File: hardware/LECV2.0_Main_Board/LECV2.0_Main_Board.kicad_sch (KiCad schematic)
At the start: 21 parts, among them J1 LED Indicator Connector, J10 Conn_01x02, J12 Radio, J2 Ox Main, J3 Fuel Main, J4 DAQ HAT Connector, U1 Pico, U2 INA237_Module, U4 W25Q128JVSIQ, U5 Adafruit LSM6DSOX + LIS3MDL

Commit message: Added name to schematic
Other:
- company: (none) -> Missouri S&T Rocket Design Team
- title: (none) -> LECV2.0 Main Board
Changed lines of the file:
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@@
 	(generator_version "9.0")
 	(paper "A3")
+	(title_block
+		(title "LECV2.0 Main Board")
+		(company "Missouri S&T Rocket Design Team")
+		(comment 1 "Author: Rakshak Sudhakaran")
+	)
 	(rectangle
 		(start 170.18 199.39)

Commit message: Temp commit to upload changes to buck converter circuit
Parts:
- added C11: 150u, EEUFC1H151B:CAPPRD500W60D1000H1600, symbol Device:C_Polarized
- added C9: 220n, Capacitor_SMD:C_0805_2012Metric, symbol Device:C
- added R7, R9: 1k, Resistor_SMD:R_0603_1608Metric, symbol Device:R_US
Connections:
- net 11.1V: now also C11.1, C9.1
- net GND: now also C11.2
- net at J3.3 (Pin_3), R1.1: now also R9.2; no longer U1.27 (GPIO21)
- net at J2.3 (Pin_3), R3.1: now also R7.2; no longer U1.29 (GPIO22)
- net at J10.2 (Pin_2), U2. (Vin+): now also C9.2
- new net: R9.1, U1.27 (GPIO21)
- new net: R7.1, U1.29 (GPIO22)
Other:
- moved on the sheet: C18, C22, C24, D1, J1, J10, J2, J3, J4, MOSFET1, R1, R2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

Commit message: Implemented fixes. Ready for 2nd review
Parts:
- added F1: Fuse, Fuse:Fuse_1206_3216Metric, symbol Device:Fuse
- added Q1: BUK6Y33-60PX, BUK6Y33-60PX:LFPAK_SOT669_NEX, symbol BUK6Y33-60PX:BUK6Y33-60PX
- added Q2: Q_NPN, Package_TO_SOT_SMD:SOT-323_SC-70, symbol Device:Q_NPN
- R7, R9: value 1k -> 10K; DigiKey https://www.digikey.com/en/products/detail/vishay-dale/TNPW06031K00BEEA/1606767 -> https://www.digikey.com/en/products/detail/vishay-dale/TNPW060310K0BEEA/1606881
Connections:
- net 11.1V: now also R9.1, Q1.1 (S), Q1.2 (S), Q1.3 (S); no longer C18.1, C22.1, J2.1 (Pin_1), J3.1 (Pin_1)
- net GND: now also Q2.E
- net at J3.3 (Pin_3), R1.1: now also U1.27 (GPIO21); no longer R9.2
- net at J2.3 (Pin_3), R3.1: now also U1.29 (GPIO22); no longer R7.2
- net at R7.1: now also Q2.B; no longer U1.29 (GPIO22)
- net GPIO0 (Servo_PWR_Switch): now reaches U1.4 (GPIO2)
- net GPIO0 (Servo_PWR_Switch): now also R7.2
- new net: Q1.4 (G), Q2.C, R9.2
- new net: C18.1, C22.1, J2.1 (Pin_1), J3.1 (Pin_1), Q1.5 (D)
- new net: C9.2, F1.1, U2. (Vin+)
- new net: F1.2, J10.2 (Pin_2)
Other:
- note added: "Servomotor Power Switch"
- moved on the sheet: C18, C22, C3, J10, J12, J2, J3, U4

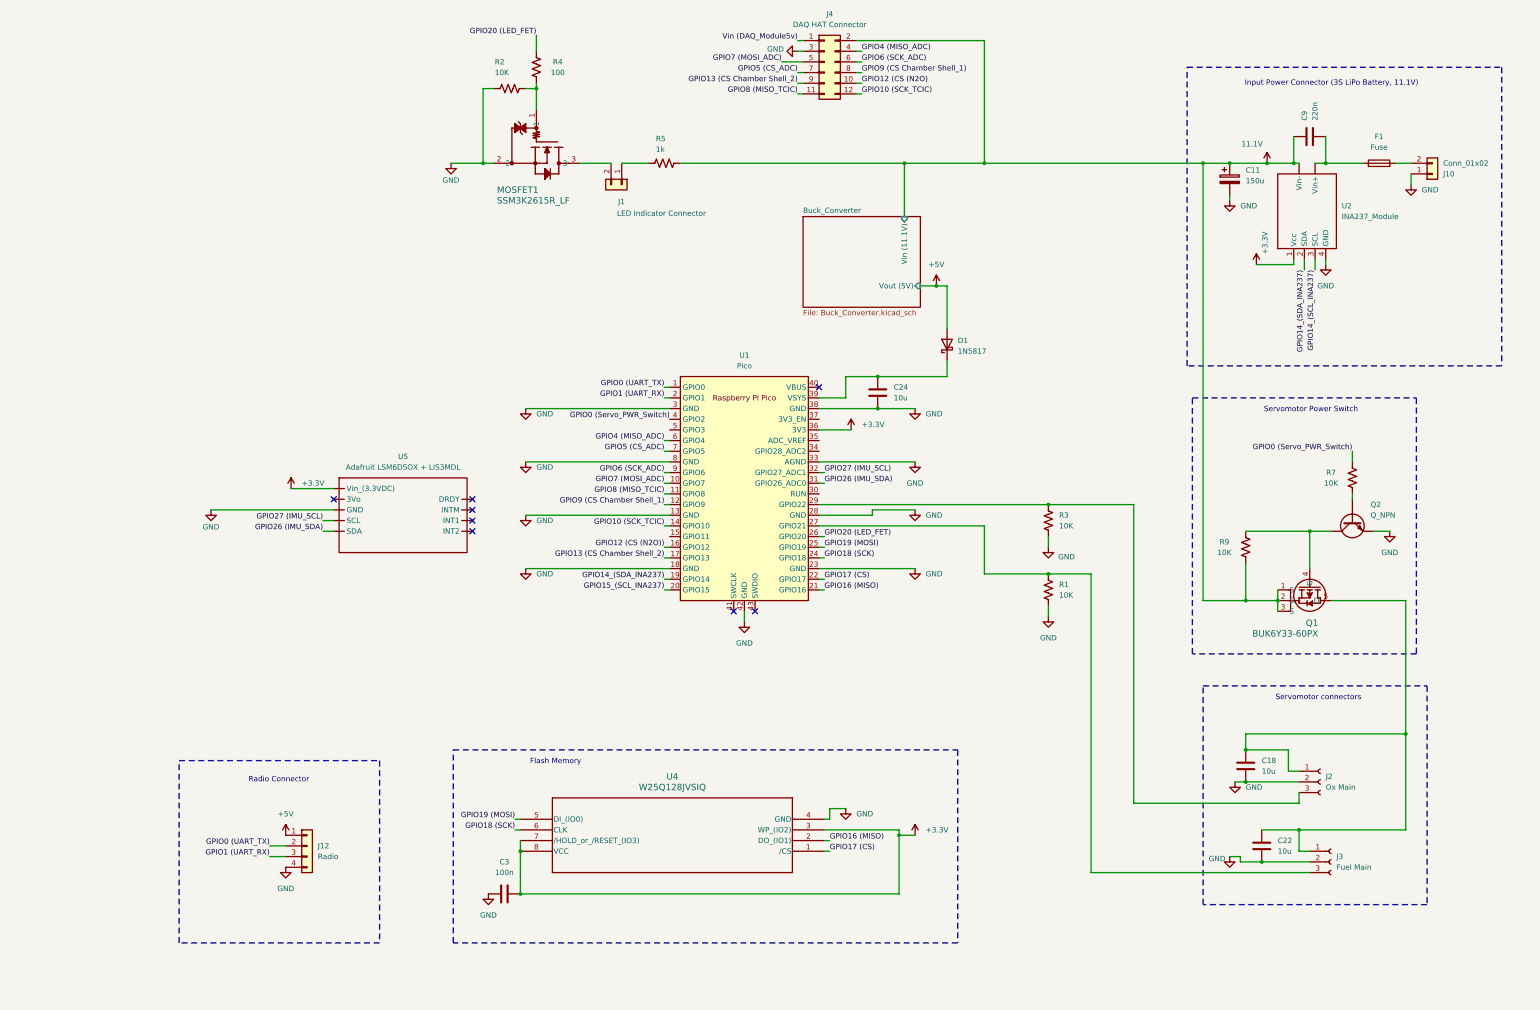
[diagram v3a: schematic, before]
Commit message: Intermediate commit, need to fix servo connector footprints
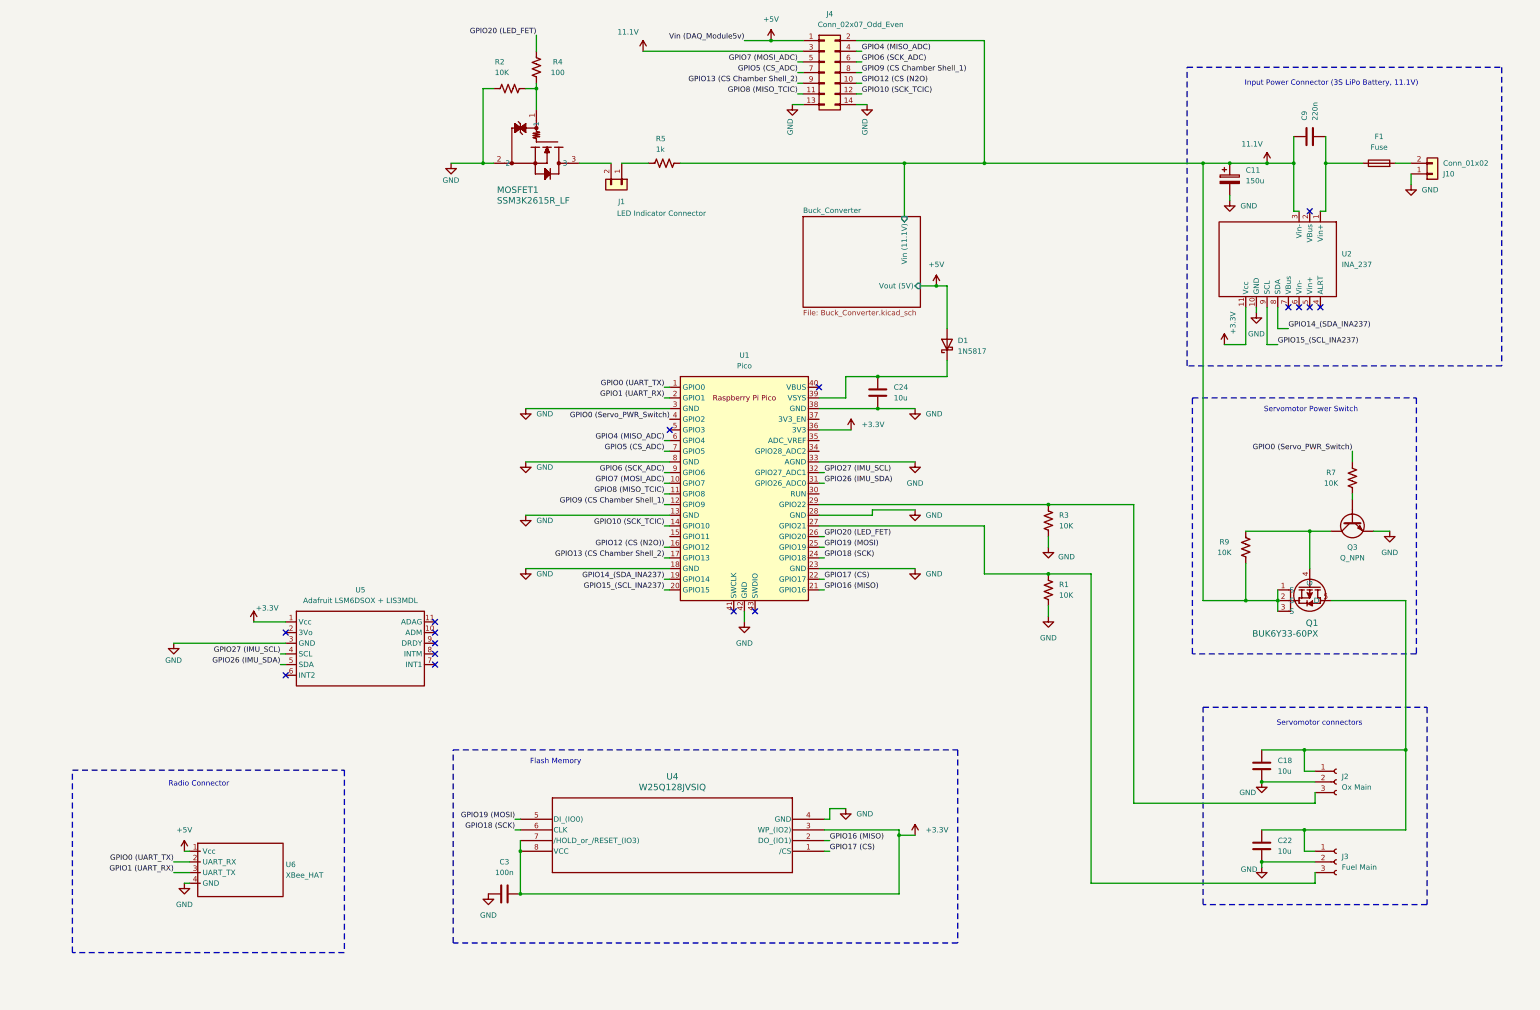
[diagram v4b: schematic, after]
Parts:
- removed J12: Radio, symbol Connector_Generic:Conn_01x04
- removed J4: DAQ HAT Connector, Connector_PinHeader_2.54mm:PinHeader_2x06_P2.54mm_Vertical, symbol Connector_Generic:Conn_02x06_Odd_Even
- removed Q2: Q_NPN, Package_TO_SOT_SMD:SOT-323_SC-70, symbol Device:Q_NPN
- added J4: Conn_02x07_Odd_Even, Connector_PinHeader_2.54mm:PinHeader_2x07_P2.54mm_Vertical, symbol Connector_Generic:Conn_02x07_Odd_Even
- added Q3: Q_NPN, Package_TO_SOT_SMD:SOT-323_SC-70, symbol Device:Q_NPN
- added U6: XBee_HAT, XBee_HAT:XBee-HAT, symbol XBee_HAT:XBee_HAT
- J2, J3: footprint (none) -> Connector_PinHeader_2.54mm:PinHeader_1x03_P2.54mm_Vertical
- U2: value INA237_Module -> INA_237; footprint (none) -> INA_238:INA238_MODULE
- U5: footprint (none) -> Adafruit_LSM6DSOX+LIS3MDL:Adafruit_LSM6DSOX+LIS3MDL
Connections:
- net GPIO14_(SCL_INA237) is gone; now on net 11.1V: U2.3 (Vin-)
- net +3.3V: now also U2.11 (Vcc), U5.1 (Vcc); no longer U2.1 (Vcc), U5. (INT2)
- net +5V: now also J4.1 (Pin_1), U6.1 (Vcc)
- net 11.1V: now also J4.2 (Pin_2), J4.3 (Pin_3); no longer U2. (Vin+)
- net GND: now also U2.10 (GND), U5.3 (GND), J4.13 (Pin_13), J4.14 (Pin_14), Q3.2 (E), U6.4 (GND); no longer U2.4 (GND), U5. (INT2)
- net GPIO0 (UART_TX): now also U6.2 (UART_RX)
- net GPIO1 (UART_RX): now also U6.3 (UART_TX)
- net GPIO10 (SCK_TCIC): now also J4.12 (Pin_12)
- net GPIO12 (CS (N2O): now also J4.10 (Pin_10)
- net GPIO13 (CS Chamber Shell_2): now also J4.9 (Pin_9)
- net GPIO14_(SDA_INA237): now also U2.8 (SDA); no longer U2.2 (SDA)
- net GPIO15_(SCL_INA237): now also U2.9 (SCL)
- net GPIO26 (IMU_SDA): now also U5.5 (SDA); no longer U5. (INT2)
- net GPIO27 (IMU_SCL): now also U5.4 (SCL); no longer U5. (INT2)
- net GPIO4 (MISO_ADC): now also J4.4 (Pin_4)
- net GPIO5 (CS_ADC): now also J4.7 (Pin_7)
- net GPIO6 (SCK_ADC): now also J4.6 (Pin_6)
- net GPIO7 (MOSI_ADC): now also J4.5 (Pin_5)
- net GPIO8 (MISO_TCIC): now also J4.11 (Pin_11)
- net GPIO9 (CS Chamber Shell_1): now also J4.8 (Pin_8)
- net at Q1.4 (G), R9.2: now also Q3.3 (C)
- net at C9.2, F1.1: now also U2.1 (Vin+); no longer U2. (Vin+)
- net at R7.1: now also Q3.1 (B)
- no-connect marks 8 -> 16
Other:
- moved on the sheet: C18, J2, J3

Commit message: Fixed all footprints. Defined PCB edge, arbitrarily placed components
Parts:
- J2, J3: footprint Connector_PinHeader_2.54mm:PinHeader_1x03_P2.54mm_Vertical -> 54-00440:TENSILITY_54-00440; DigiKey (none) -> https://www.digikey.com/en/products/detail/tensility-intern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
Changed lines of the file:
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@@
 			)
 		)
-		(property "Footprint" "Connector_PinHeader_2.54mm:PinHeader_1x03_P2.54mm_Vertical"
+		(property "Footprint" "54-00440:TENSILITY_54-00440"
 			(at 358.14 203.2 0)
 			(effects
@@
 			)
 		)
-		(property "Datasheet" "~"
+		(property "Datasheet" "https://tensility.s3.us-west-2.amazonaws.com/uploads/pdffiles/54-00440.pdf"
 			(at 358.14 203.2 0)
 			(effects
@@
 		)
 		(property "Description" "Generic connector, single row, 01x03, script generated"
+			(at 358.14 203.2 0)
+			(effects
+				(font
+					(size 1.27 1.27)
+				)
+				(hide yes)
+			)
+		)
+		(property "DigiKey" "https://www.digikey.com/en/products/detail/tensility-international-corp/54-00440/26797725"
 			(at 358.14 203.2 0)
 			(effects
@@
 			)
 		)
-		(property "Footprint" "Connector_PinHeader_2.54mm:PinHeader_1x03_P2.54mm_Vertical"
+		(property "Footprint" "54-00440:TENSILITY_54-00440"
 			(at 358.14 222.25 0)
 			(effects
@@
 			)
 		)
-		(property "Datasheet" "~"
+		(property "Datasheet" "https://tensility.s3.us-west-2.amazonaws.com/uploads/pdffiles/54-00440.pdf"
 			(at 358.14 222.25 0)
 			(effects
@@
 			(at 358.14 222.25 0)
 			(effects
+				(font
+					(size 1.27 1.27)
+				)
+				(hide yes)
+			)
+		)
+		(property "DigiKey" "https://www.digikey.com/en/products/detail/tensility-international-corp/54-00440/26797725"
+			(at 358.14 222.25 0)
+			(effects

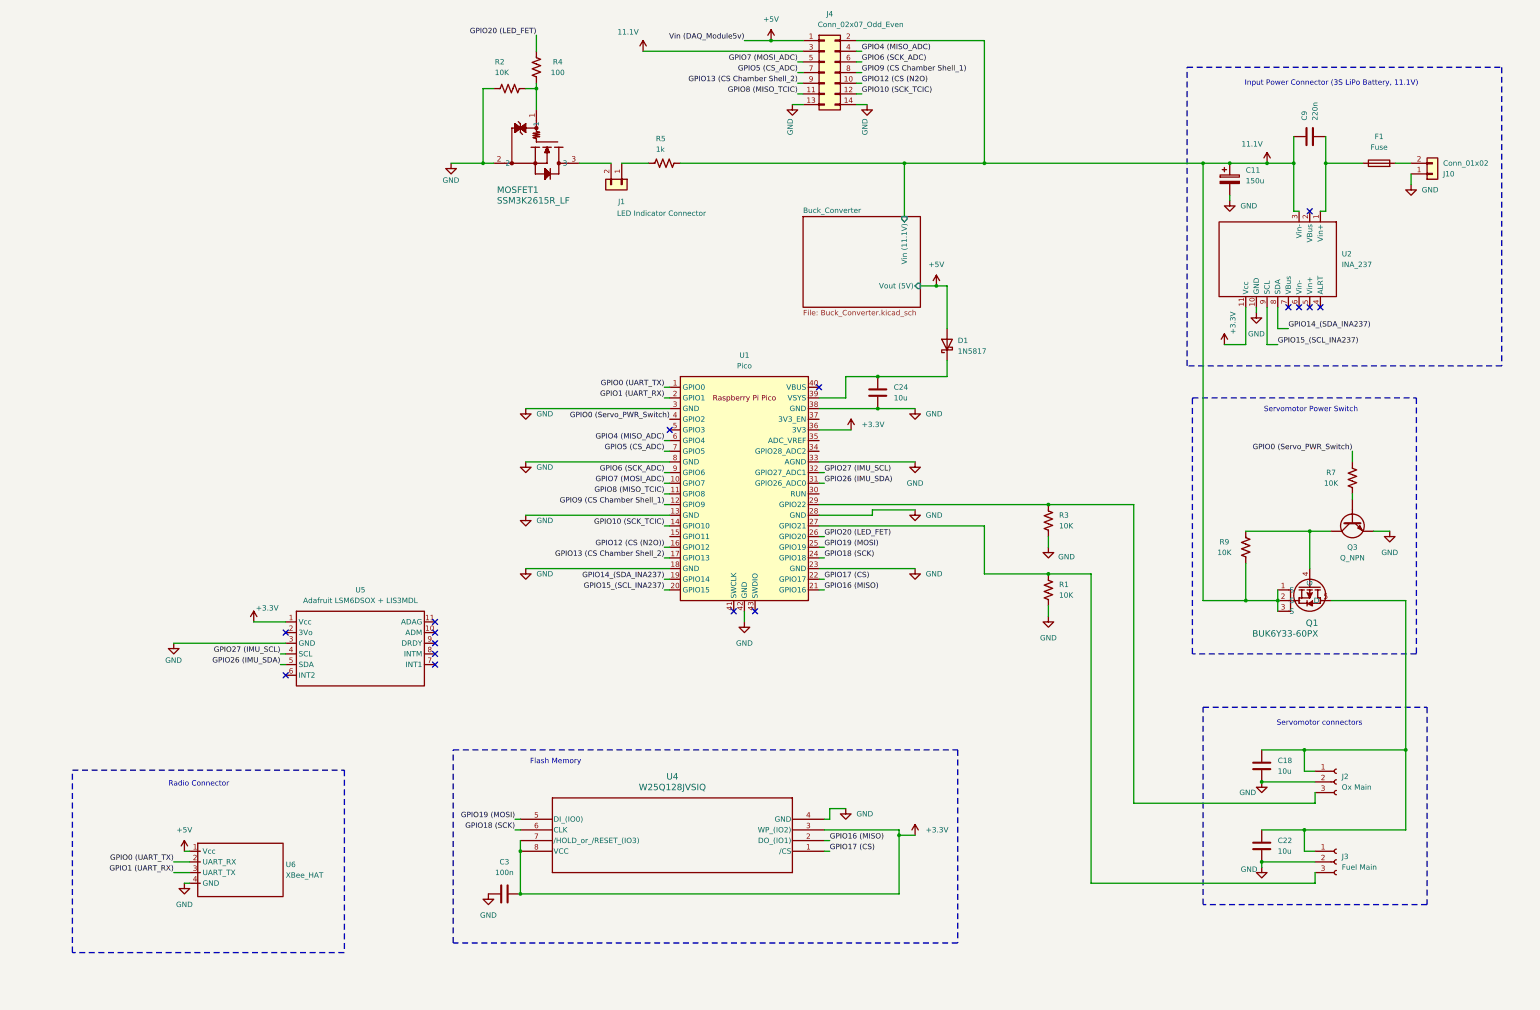
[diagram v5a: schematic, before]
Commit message: Added GPIO clamping diodes, sufficient buck output capacitance, UVLO divider, and 3V3_EN diode
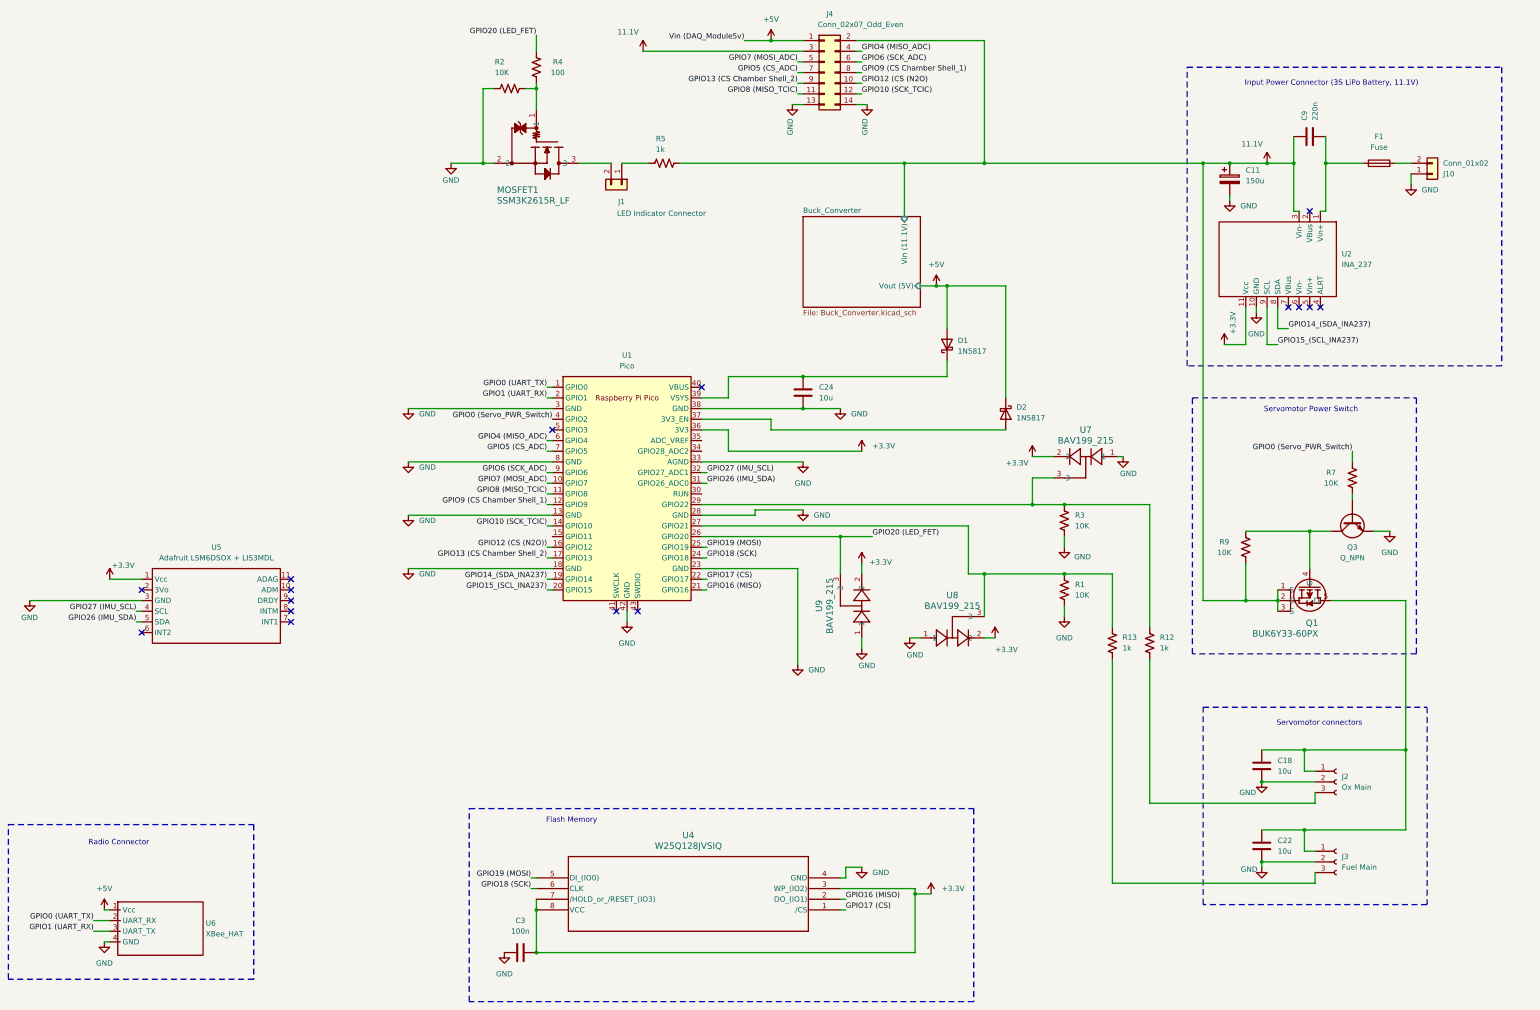
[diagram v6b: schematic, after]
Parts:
- added D2: 1N5817, Diode_THT:D_DO-41_SOD81_P10.16mm_Horizontal, symbol Diode:1N5817
- added R12, R13: 1k, Resistor_SMD:R_0603_1608Metric, symbol Device:R_US
- added U7, U8, U9: BAV199_215, Package_TO_SOT_SMD:SOT-23-3, symbol BAV199_215:BAV199_215
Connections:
- net +3.3V: now also U7.2, U8.2, U9.2
- net +5V: now also D2.1 (K)
- net GND: now also U7.1, U8.1, U9.1
- net GPIO20 (LED_FET): now also U9.3
- net at R1.1, U1.27 (GPIO21): now also R13.1, U8.3; no longer J3.3 (Pin_3)
- net at R3.1, U1.29 (GPIO22): now also R12.1, U7.3; no longer J2.3 (Pin_3)
- net at U1.37 (3V3_EN): now also D2.2 (A)
- new net: J2.3 (Pin_3), R12.2
- new net: J3.3 (Pin_3), R13.2
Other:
- moved on the sheet: C24, C3, R1, R3, U1, U4, U5, U6

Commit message: Finished PCBs
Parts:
- removed C22, C24: 10u, Capacitor_SMD:C_0805_2012Metric, symbol Device:C
- removed D1, D2: 1N5817, Diode_THT:D_DO-41_SOD81_P10.16mm_Horizontal, symbol Diode:1N5817
- removed U9: BAV199_215, Package_TO_SOT_SMD:SOT-23-3, symbol BAV199_215:BAV199_215
- added C16, C17: 10u, Capacitor_SMD:C_1210_3225Metric, symbol Device:C
- added D3: D_Dual_Series_AKC_Parallel, Package_TO_SOT_SMD:SOT-23, symbol Device:D_Dual_Series_AKC_Parallel
- C18: footprint Capacitor_SMD:C_0805_2012Metric -> Capacitor_SMD:C_1210_3225Metric; DigiKey https://www.digikey.com/en/products/detail/samsung-electro-mechanics/CL21A106KAYNNNE/3888549 -> https://www.digikey.com/en/products/detail/samsung-electro-mechanics/CL32B106KBJNNNE/3889045
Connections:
- net GPIO12 (CS (N2O)) is gone; now on net GPIO12 (CS N2O): U1.16 (GPIO12)
- net +5V: now also J4.2 (Pin_2), U6.4 (VCC), D3.3 (common); no longer J4.1 (Pin_1), U6.1 (Vcc)
- net 11.1V: now also J4.1 (Pin_1); no longer J4.2 (Pin_2), J4.3 (Pin_3)
- net GND: now also U6.1 (GND), C16.2, C17.2; no longer U6.4 (GND)
- net at R1.1, R13.1, U8.3: now also U1.31 (GPIO26_ADC0); no longer U1.27 (GPIO21)
- net SrvoPwr (11.1V): now reaches J2.1 (Pin_1), J3.1 (Pin_1), Q1.5 (D)
- net SrvoPwr (11.1V): now also C16.1, C17.1; no longer C18.1
- net at R12.1, R3.1, U7.3: now also U1.32 (GPIO27_ADC1); no longer U1.29 (GPIO22)
- net Vin+ (INA237): now reaches C9.2, F1.1, U2.1 (Vin+)
- net +BATT: now reaches F1.2, J10.2 (Pin_2)
- net at U1.37 (3V3_EN): now also D3.1 (A)
- net at U1.39 (VSYS): now also C18.1, D3.2 (K)
- net GPIO28 (Servo_PWR_Switch): now reaches U1.34 (GPIO28_ADC2)
- net GPIO28 (Servo_PWR_Switch): now also R7.2
- net GPIO3 (IMU_SCL): now reaches U1.5 (GPIO3)
- net GPIO3 (IMU_SCL): now also U5.4 (SCL)
- net GPIO0 (Servo_PWR_Switch) renamed GPIO2 (IMU_SDA)
- net GPIO2 (IMU_SDA): now also U5.5 (SDA); no longer R7.2
- net GPIO0 (UART_TX) renamed GPIO0 (Pico_TX)
- net GPIO0 (Pico_TX): now also U6.3 (UART_RX); no longer U6.2 (UART_RX)
- net GPIO1 (UART_RX) renamed GPIO1 (Pico_RX)
- net GPIO1 (Pico_RX): now also U6.2 (UART_TX); no longer U6.3 (UART_TX)
- net GPIO12 (CS (N2O) renamed GPIO12 (CS N2O)
- net GPIO14_(SDA_INA237) renamed GPIO14 (FanCtrl)
- net GPIO14 (FanCtrl): now also J4.3 (Pin_3); no longer U2.8 (SDA)
- net GPIO15_(SCL_INA237): no longer names the net of U1.20 (GPIO15)
- net GPIO15_(SCL_INA237): no longer U2.9 (SCL)
- net GPIO20 (LED_FET) renamed GPIO20_(SDA_INA237)
- net GPIO20_(SDA_INA237): now also U2.8 (SDA); no longer R4.1
- removed net GPIO26 (IMU_SDA): U1.31 (GPIO26_ADC0), U5.5 (SDA)
- removed net GPIO27 (IMU_SCL): U1.32 (GPIO27_ADC1), U5.4 (SCL)
- new net GPIO21_(SCL_INA237): U1.27 (GPIO21), U2.9 (SCL)
- new net GPIO22 (LED_FET): R4.1, U1.29 (GPIO22)
- no-connect marks 16 -> 18
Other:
- title: LECV2.0 Main Board -> LEC Main Board
- moved on the sheet: R3
